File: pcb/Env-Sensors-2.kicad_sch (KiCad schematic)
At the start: 16 parts, among them Q1 MMBFJ201, U10 TSL2591, U13 BMP581, U14 MCP6042, U15 ADS1115, U18 TGS5141

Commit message: Rev A Updates
Support LD2410S and LD2420 Radars in same connector as C4001. Now using 3.3V instead of 5V.
Removed Power control for Radars.
Added DS18S20 to measure CO sensor temperature directly.
Reworked SHT4X layout to reduce thermal transfer.
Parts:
- added U17: DS18S20, Package_TO_SOT_THT:TO-92_Inline, symbol Sensor_Temperature:DS18S20
- renumbered C27 to C23, C32 to C28, C33 to C29, C35 to C31, C37 to C33, C39 to C35, C41 to C37, R17 to R15, R18 to R16, U13 to U11, U14 to U12, U15 to U13, U18 to U16, U10 to U8
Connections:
- net +3.3VA: now also U17.3 (V_{DD})
- net GND: now also U17.1 (GND)
- new net 1Wire: U17.2 (DQ)

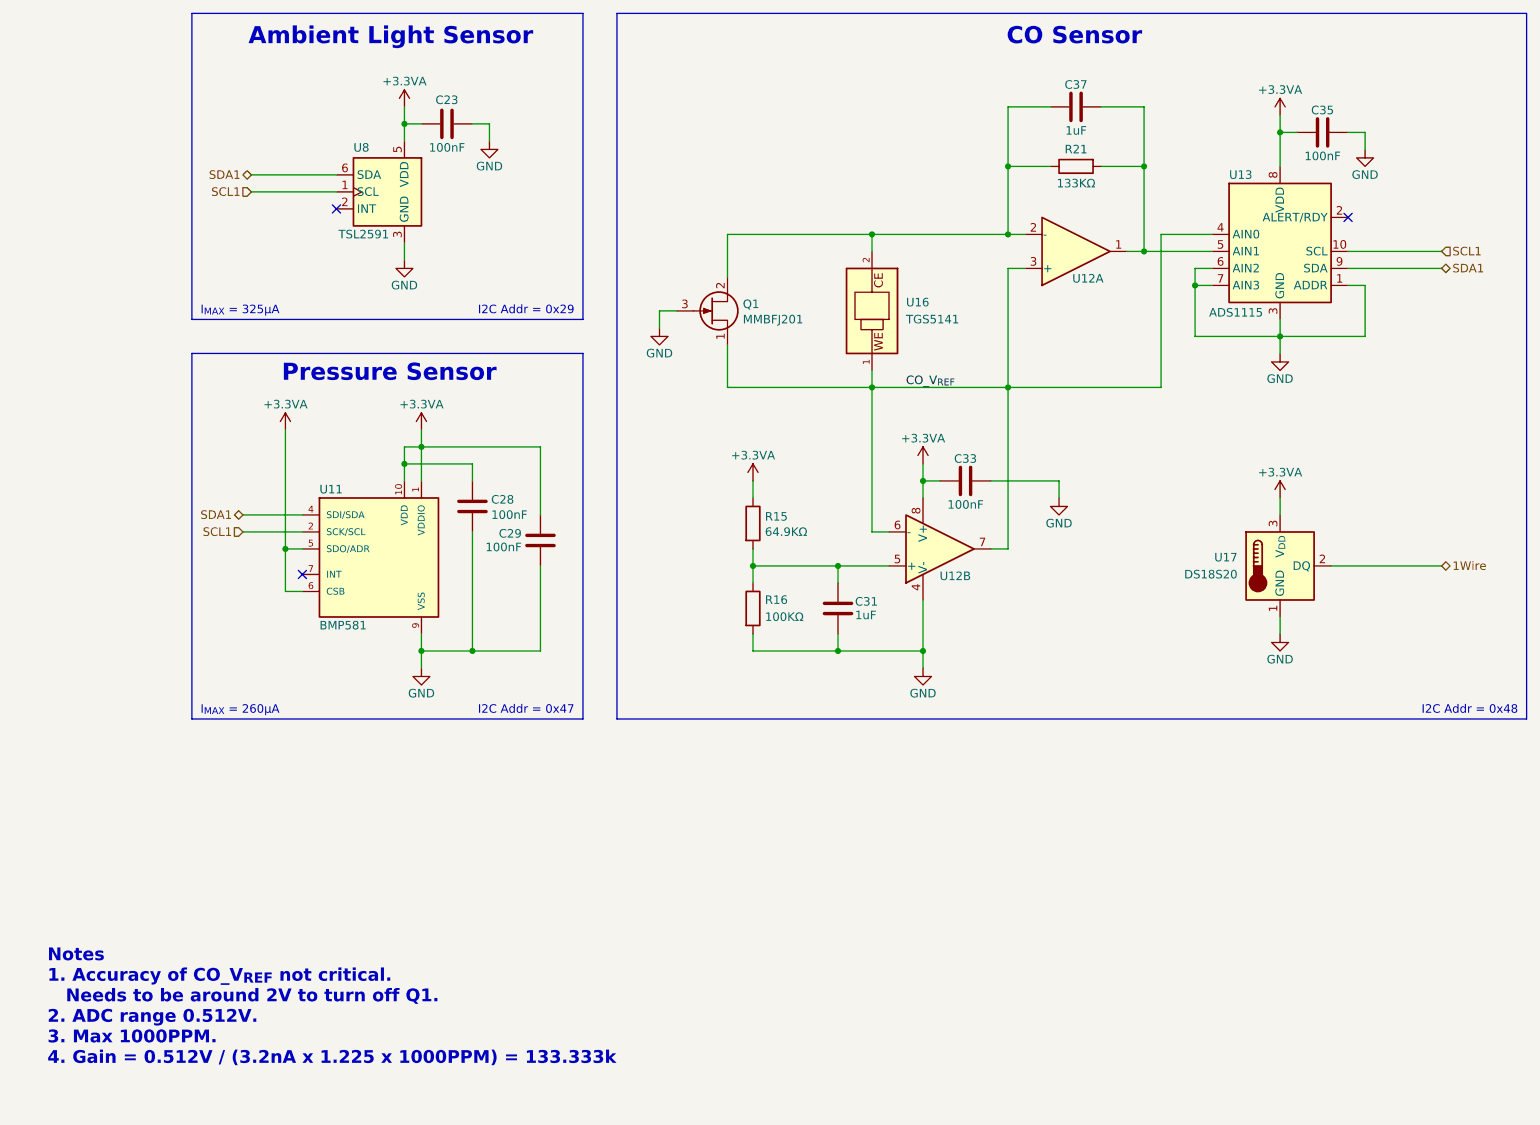
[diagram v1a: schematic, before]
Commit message: Rev B Updates finish adding power monitors for 3.3V and 3.3VA
Removed speaker gain jumper
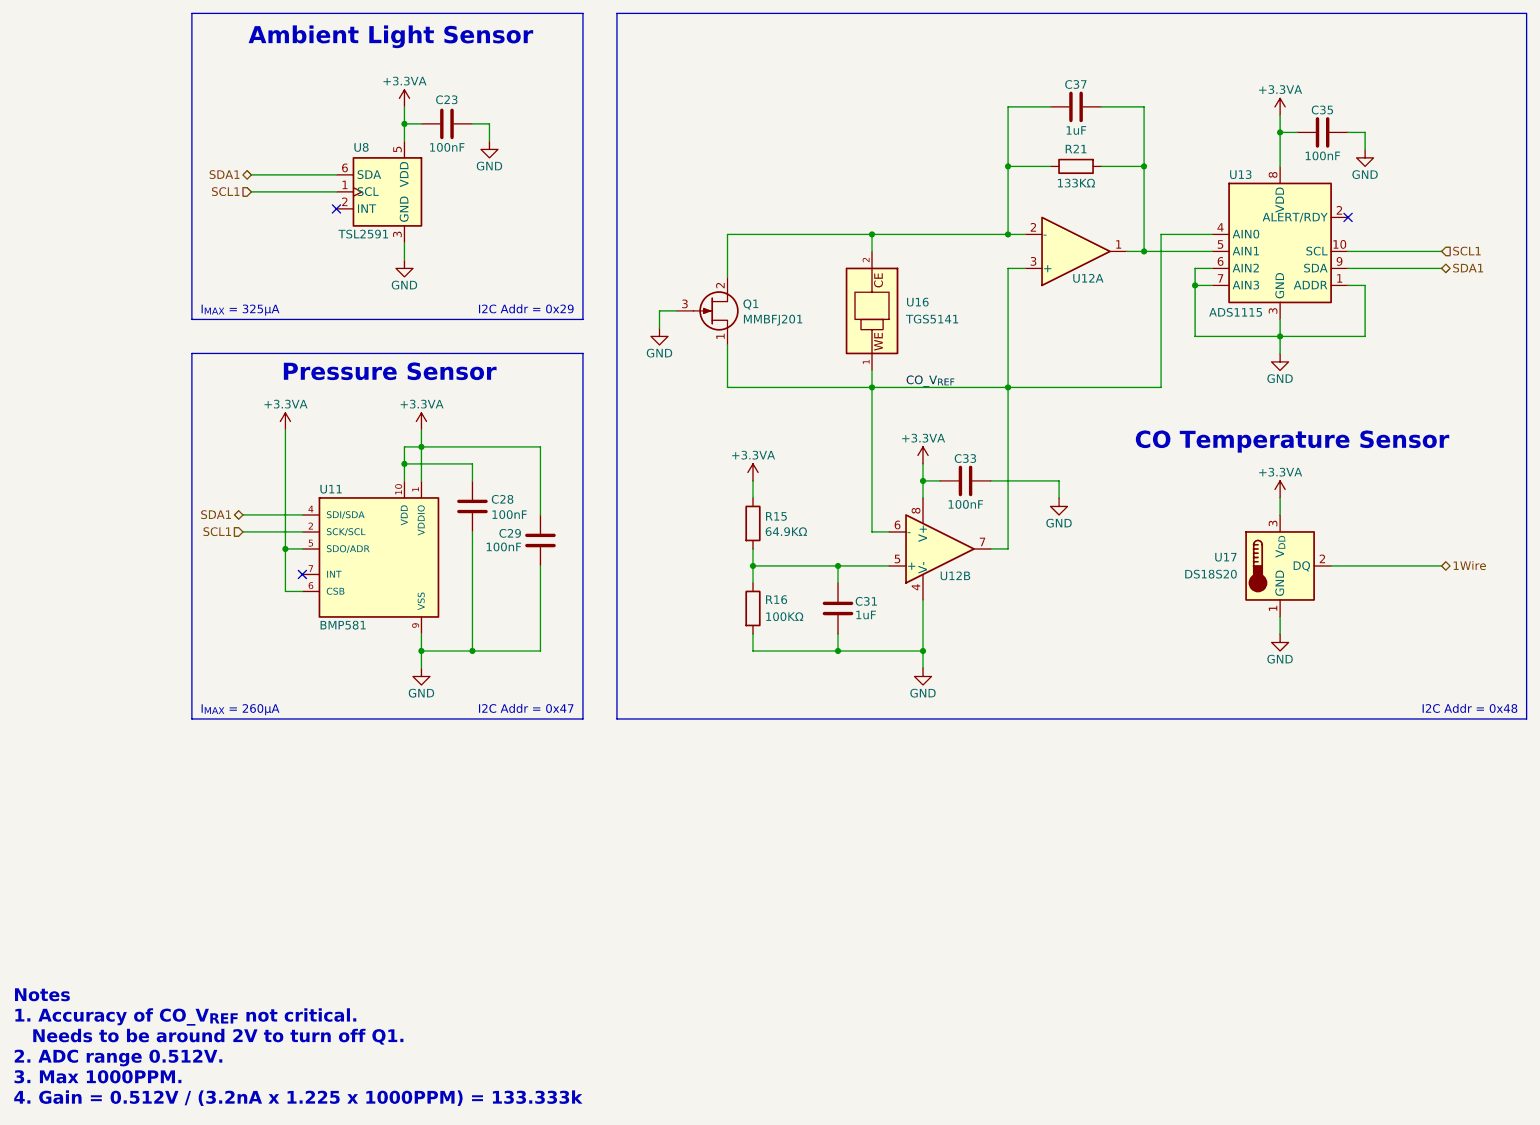
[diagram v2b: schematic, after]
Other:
- note added: "CO Temperature Sensor"
- note removed: "CO Sensor"
- title: ESPHome Parking Assistant -> ESPHome Indoor Multi-Sensor
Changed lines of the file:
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@@
 	(generator "eeschema")
 	(generator_version "9.0")
-	(paper "A4")
+	(paper "A")
 	(title_block
-		(title "ESPHome Parking Assistant")
-		(date "2025-09-23")
+		(title "ESPHome Indoor Multi-Sensor")
+		(date "2025-09-24")
 		(rev "B")
 		(company "Mike Lawrence")
@@
 		)
 	)
-	(text "CO Sensor"
+	(text "CO Temperature Sensor"
 		(exclude_from_sim no)
-		(at 178.816 27.432 0)
+		(at 211.328 87.884 0)
 		(effects
 			(font
@@
 	(text "Notes\n1. Accuracy of CO_V_{REF} not critical. \n   Needs to be around 2V to turn off Q1.\n2. ADC range 0.512V.\n3. Max 1000PPM.\n4. Gain = 0.512V / (3.2nA x 1.225 x 1000PPM) = 133.333k"
 		(exclude_from_sim no)
-		(at 25.4 165.1 0)
+		(at 20.32 171.196 0)
 		(effects
 			(font
